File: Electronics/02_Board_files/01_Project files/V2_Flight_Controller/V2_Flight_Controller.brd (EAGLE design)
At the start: 40 x 40 mm, 75 parts

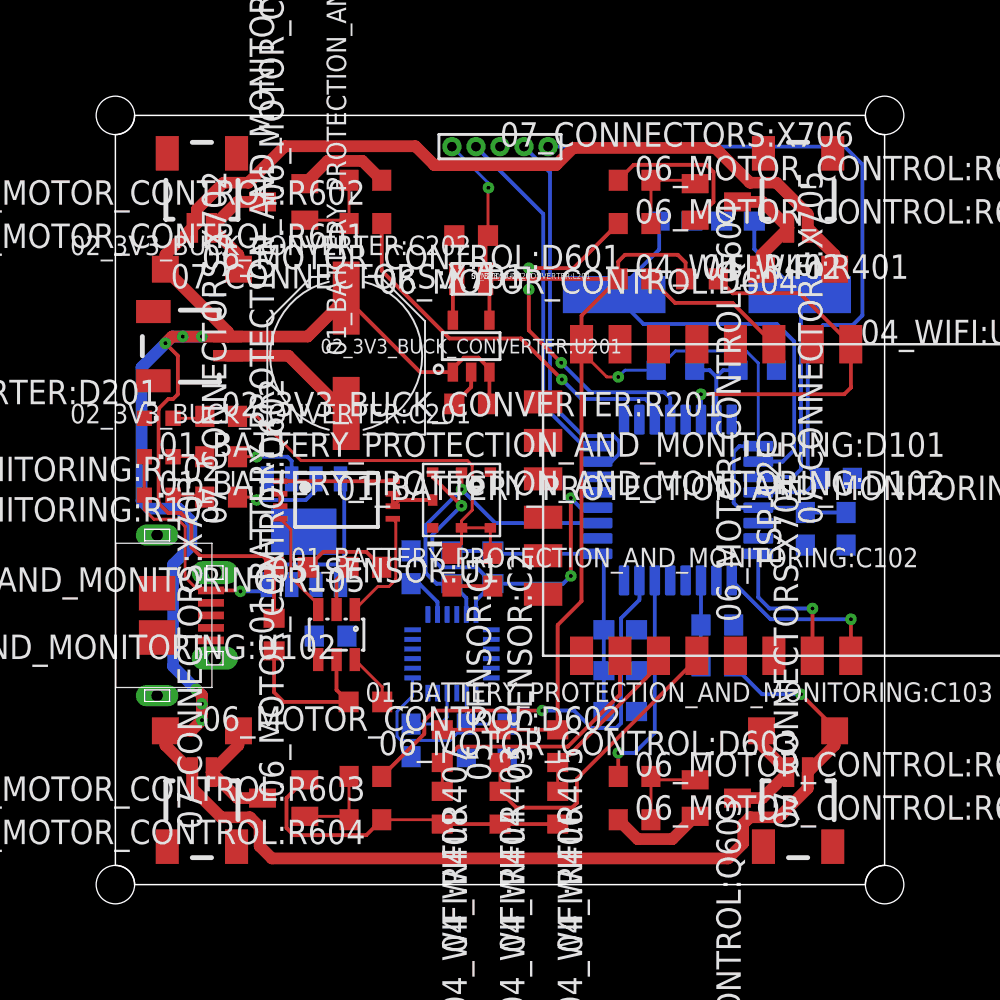
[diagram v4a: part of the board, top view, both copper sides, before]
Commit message: 1. Minor changes in a few libraries 2. Completed whole routing, DRC remaining 3. Added no connect library
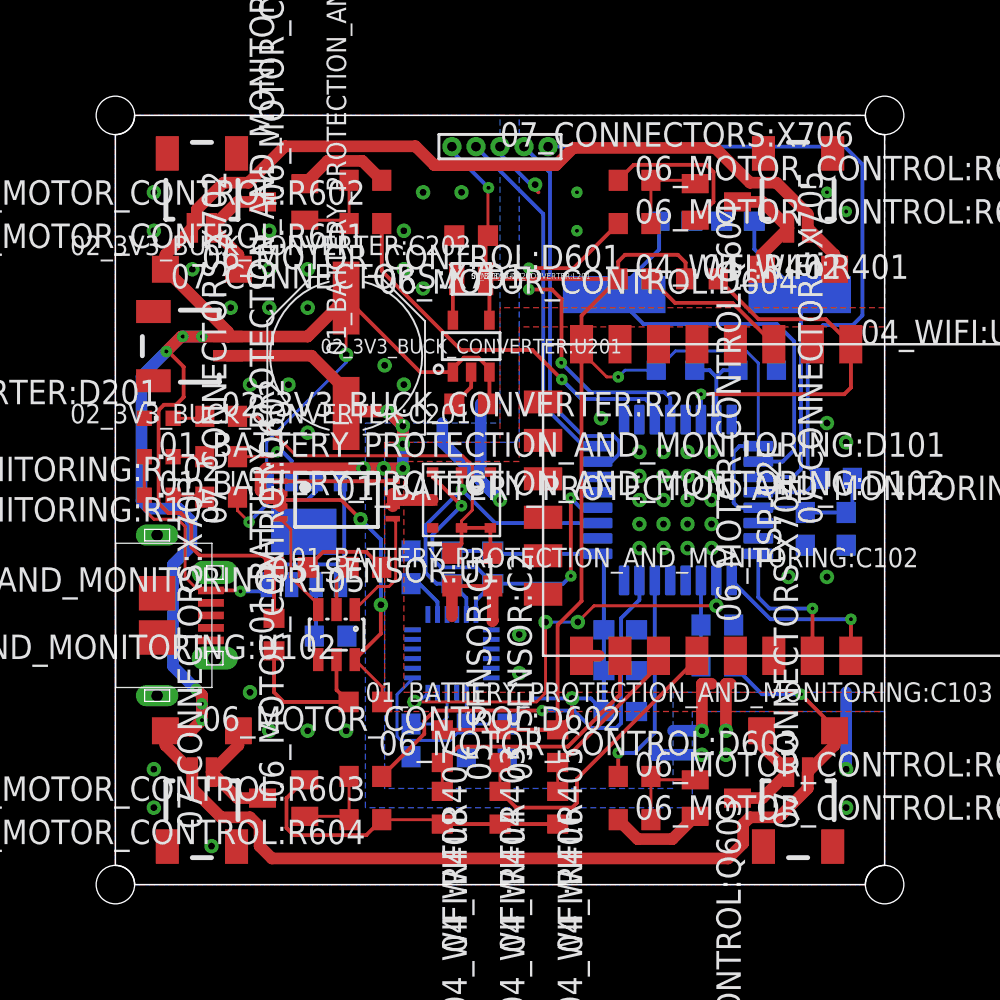
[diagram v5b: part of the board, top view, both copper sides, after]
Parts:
- 02_3V3_BUCK_CONVERTER:C201: value (none) -> 10nF
- 02_3V3_BUCK_CONVERTER:C202: value (none) -> 10uF
- 02_3V3_BUCK_CONVERTER:R201, 06_MOTOR_CONTROL:R601, 06_MOTOR_CONTROL:R603, 06_MOTOR_CONTROL:R605, 06_MOTOR_CONTROL:R607: value (none) -> 1KΩ
- 03_MICROCONTROLLER:L302, 03_MICROCONTROLLER:L303: value (none) -> FERRITE BEAD
- 04_WIFI:U401: value (none) -> WIFI_MODULE
- 06_MOTOR_CONTROL:D601, 06_MOTOR_CONTROL:D602, 06_MOTOR_CONTROL:D603, 06_MOTOR_CONTROL:D604: value (none) -> 1N5819
- 06_MOTOR_CONTROL:Q601, 06_MOTOR_CONTROL:Q602, 06_MOTOR_CONTROL:Q603, 06_MOTOR_CONTROL:Q604: value (none) -> SI2302
- 06_MOTOR_CONTROL:R602, 06_MOTOR_CONTROL:R604, 06_MOTOR_CONTROL:R606, 06_MOTOR_CONTROL:R608: value (none) -> 4.7KΩ
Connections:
- net 01_BATTERY_PROTECTION_AND_MONITORING:N$1 renamed 01_BATTERY_PROTECTION_AND_MONITORING:OC
- net 01_BATTERY_PROTECTION_AND_MONITORING:N$2 renamed 01_BATTERY_PROTECTION_AND_MONITORING:OD
- new net 05_SENSOR:N$1: 05_SENSOR:U501.7
- new net 05_SENSOR:N$2: 05_SENSOR:U501.6
- new net 07_CONNECTORS:N$1: 07_CONNECTORS:J701.2
- new net 07_CONNECTORS:N$2: 07_CONNECTORS:J701.3
- new net 07_CONNECTORS:N$3: 07_CONNECTORS:J701.4
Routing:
- net GND: track 49.6 -> 83.8 mm, vias 0 -> 65
- net BATTERY_-VE: track 10.8 -> 44.2 mm, vias 0 -> 8
- net IMU_INT: track 0.00 -> 22.1 mm, vias 0 -> 4
- net +3V3: track 126.8 -> 141.8 mm, vias 2 -> 3
- net BATTERY_+VE: track 168.3 -> 179.2 mm, vias 7 -> 8
- net 01_BATTERY_PROTECTION_AND_MONITORING:PROG: track 0.00 -> 2.72 mm
- net 01_BATTERY_PROTECTION_AND_MONITORING:CHRG: track 4.95 -> 6.35 mm
- net M4_PWM: track 18.8 -> 19.5 mm
- added copper zone on layer 1, net GND
- added copper zone on layer 16, net GND

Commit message: 1. Completed Routing, DRC and ERC 2. Double checked all connections, names and values 3. Started with silk screen
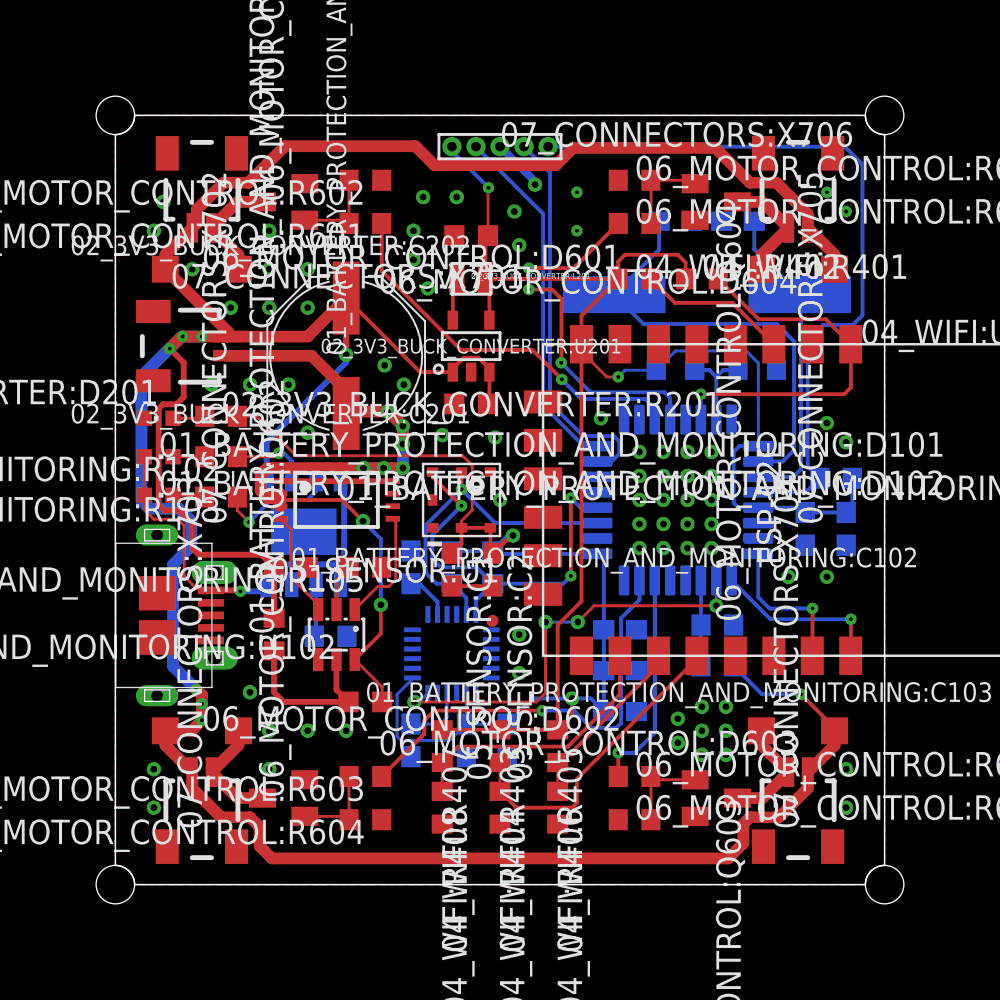
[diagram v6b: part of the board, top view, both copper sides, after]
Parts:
- 01_BATTERY_PROTECTION_AND_MONITORING:D101: value GREEN_LED -> STDBY_GREEN
- 01_BATTERY_PROTECTION_AND_MONITORING:D102: value RED_LED -> CHRG_RED
- 02_3V3_BUCK_CONVERTER:D201: value GREEN_LED -> 3V3_GREEN
- 02_3V3_BUCK_CONVERTER:L201: value SRN2009T-2R2M -> 2.2uH
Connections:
- net 01_BATTERY_PROTECTION_AND_MONITORING:N$6 renamed 01_BATTERY_PROTECTION_AND_MONITORING:D2S
- net GND: now also 07_CONNECTORS:X702.FIT@1, 07_CONNECTORS:X702.FIT@2, 07_CONNECTORS:X703.FIT@1, 07_CONNECTORS:X703.FIT@2, 07_CONNECTORS:X704.FIT@1, 07_CONNECTORS:X704.FIT@2, 07_CONNECTORS:X705.FIT@1, 07_CONNECTORS:X705.FIT@2
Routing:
- net GND: track 83.8 -> 5.53 mm, vias 65 -> 74
- net +3V3: track 141.8 -> 144.7 mm, vias 3 -> 4

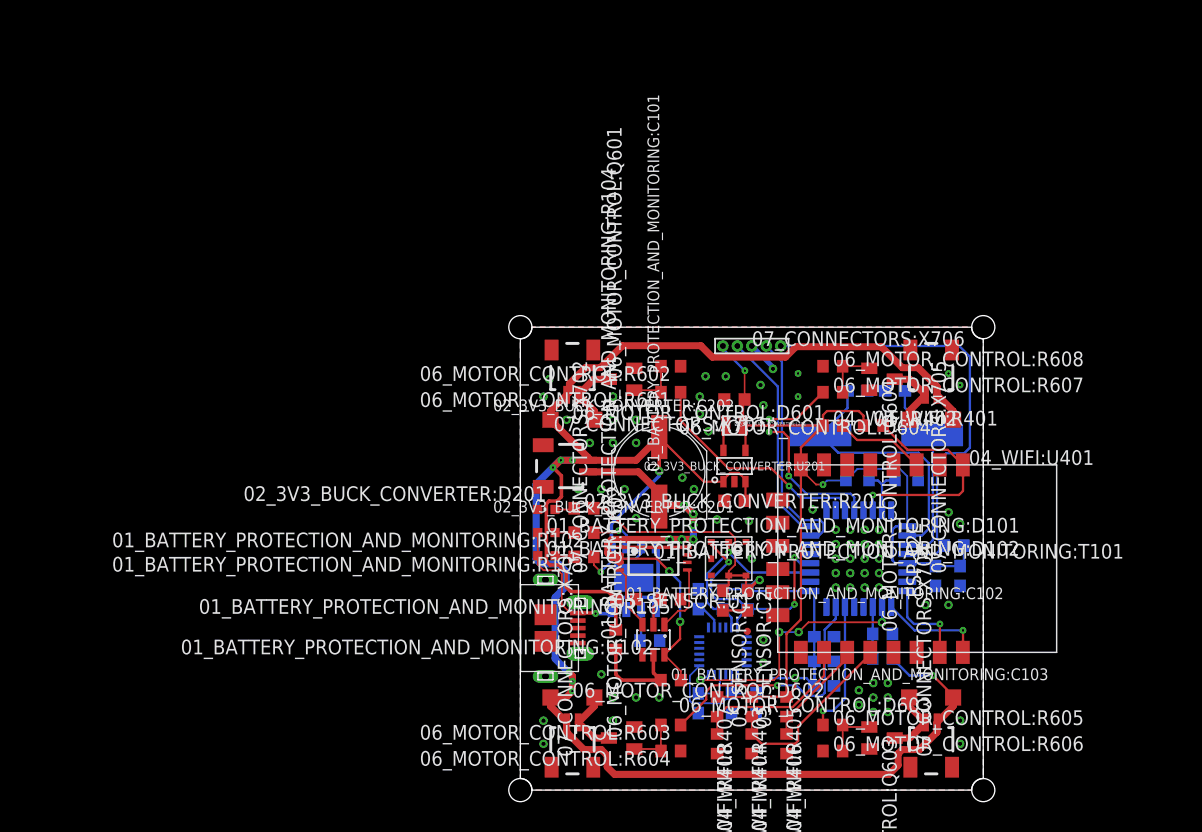
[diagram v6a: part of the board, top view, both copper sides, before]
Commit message: 1. Layer 21 tPlace changes made 2. Removed everything on Layer 51 tDocu
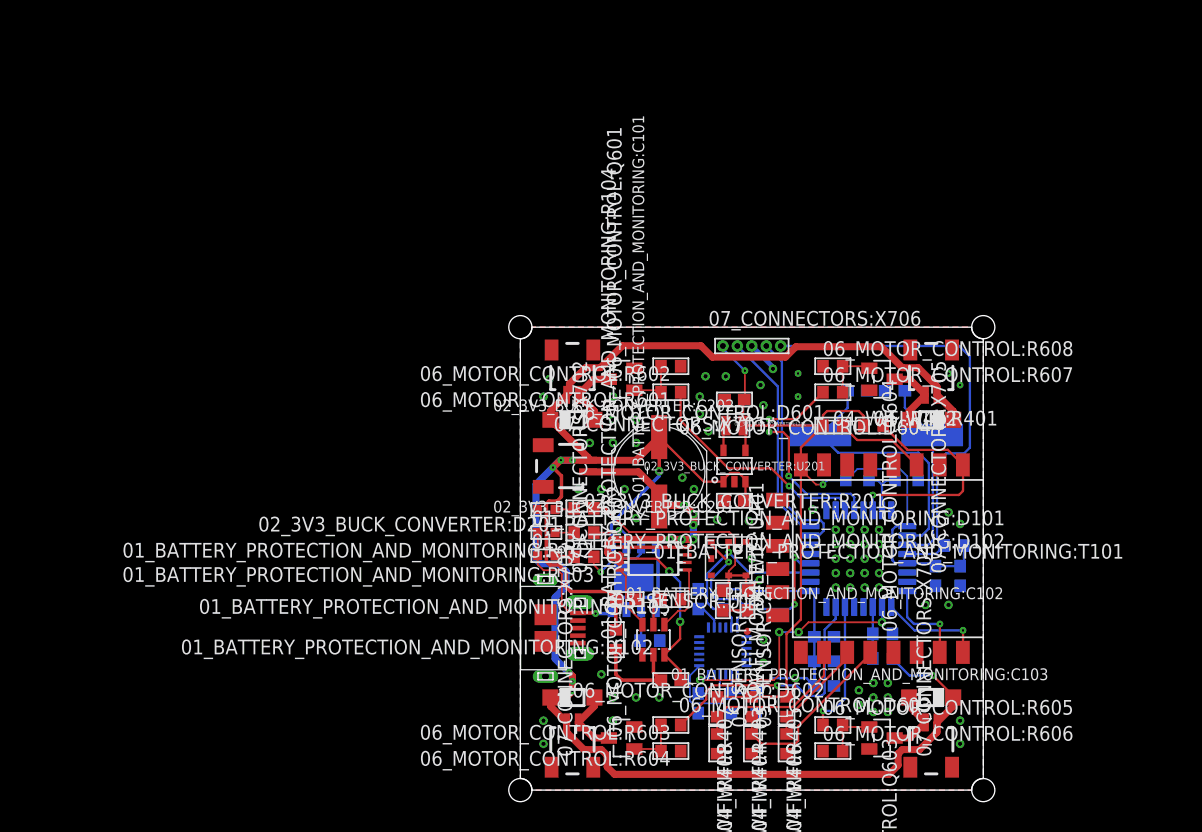
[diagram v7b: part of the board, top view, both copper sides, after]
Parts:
- 01_BATTERY_PROTECTION_AND_MONITORING:C102, 01_BATTERY_PROTECTION_AND_MONITORING:C103, 02_3V3_BUCK_CONVERTER:C201, 02_3V3_BUCK_CONVERTER:C202: device adafruit:C0603K -> adafruit:C0603

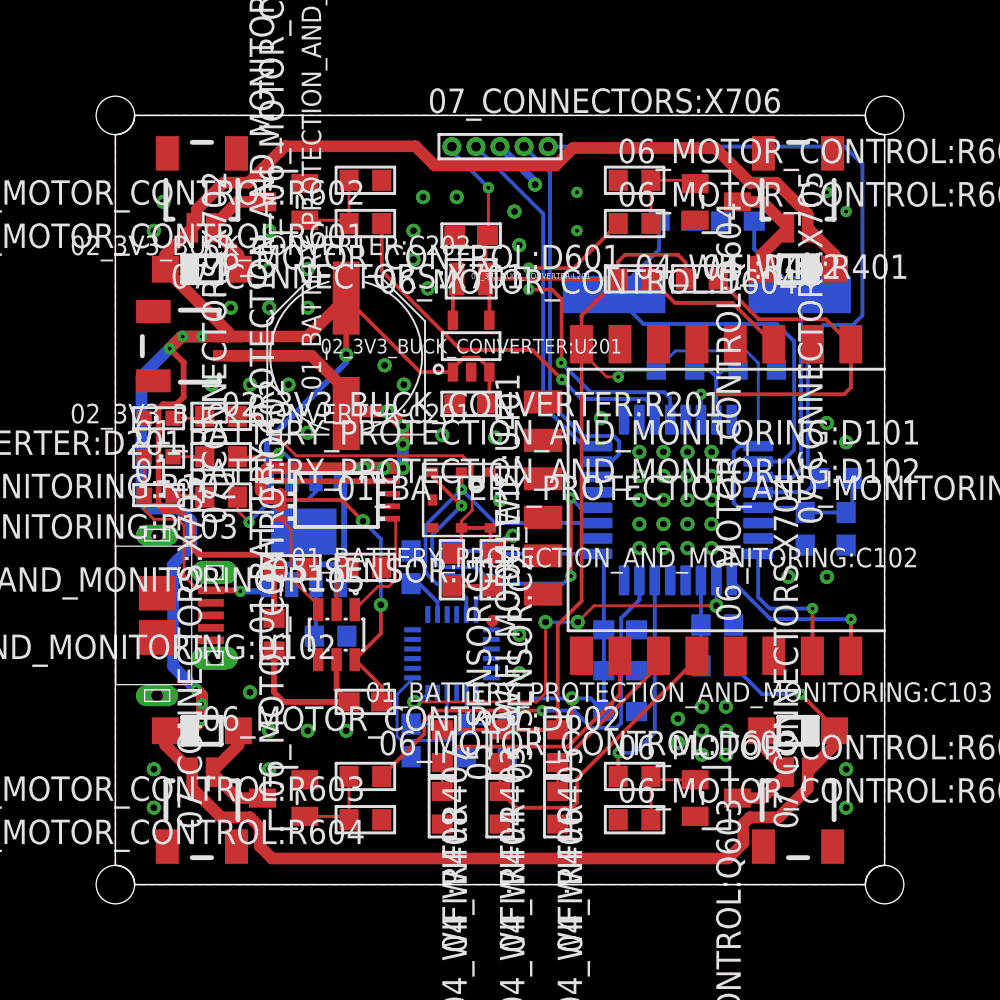
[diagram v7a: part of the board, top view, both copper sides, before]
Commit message: changed via size and filled open areas with them
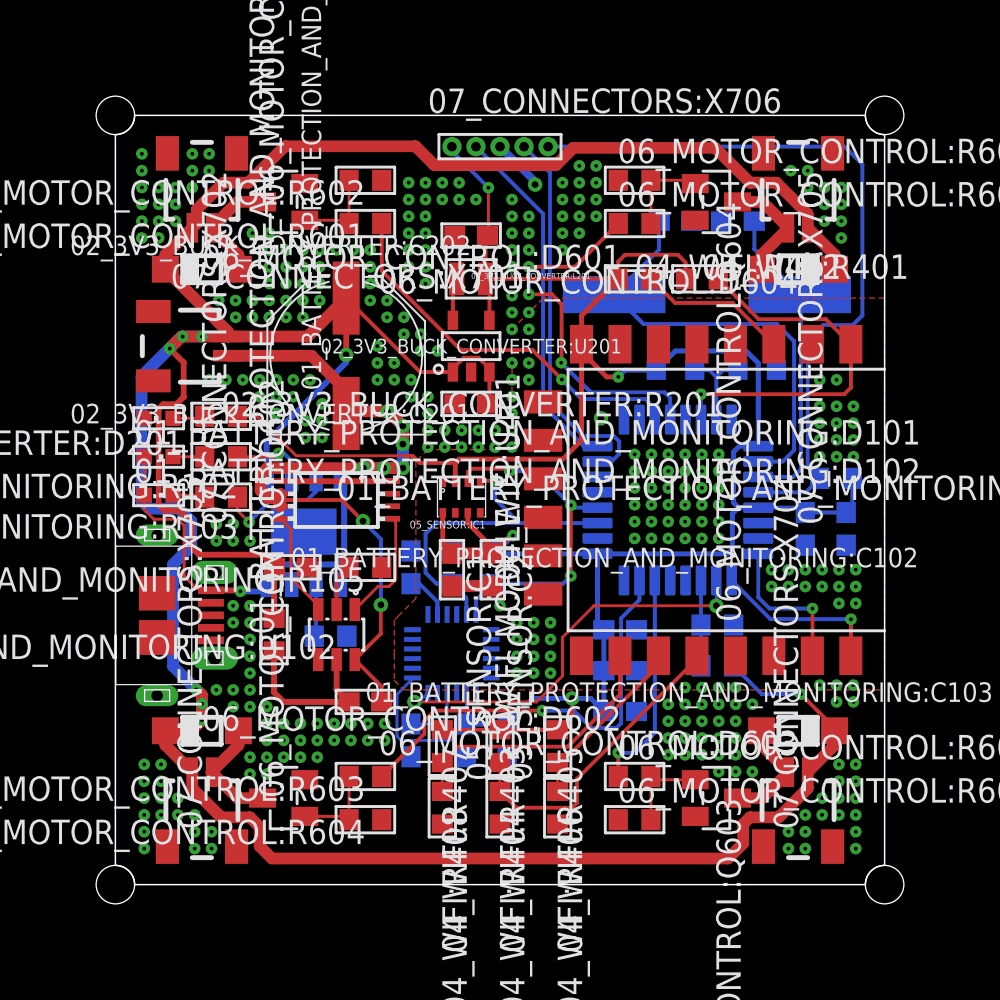
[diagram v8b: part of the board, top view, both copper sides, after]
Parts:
- removed 05_SENSOR:U1: BMP180, bmp180:BMP180
- added 05_SENSOR:IC1: BMP280, bosch-bmp280:BMP280
- 05_SENSOR:C1, 05_SENSOR:C2: value 2.2nF, 50V, ±10% -> 100nF, 50V, ±10%
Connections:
- net +3V3: now also 05_SENSOR:IC1.2, 05_SENSOR:IC1.6, 05_SENSOR:IC1.8; no longer 05_SENSOR:U1.2, 05_SENSOR:U1.3
- net GND: now also 05_SENSOR:IC1.1, 05_SENSOR:IC1.5, 05_SENSOR:IC1.7; no longer 05_SENSOR:U1.7
- net I2C_SCL: now also 05_SENSOR:IC1.4; no longer 05_SENSOR:U1.5
- net I2C_SDA: now also 05_SENSOR:IC1.3; no longer 05_SENSOR:U1.6
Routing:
- net I2C_SDA: track 21.3 -> 18.0 mm
- net +3V3: track 144.7 -> 142.6 mm
- net IMU_INT: track 22.1 -> 21.2 mm, vias 4 -> 2
- net I2C_SCL: track 17.3 -> 18.2 mm
- net GND: track 5.53 -> 5.49 mm, vias 74 -> 26
- removed copper zone on layer 16, net GND
